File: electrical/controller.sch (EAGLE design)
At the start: 27 parts, among them Q1 IRLIB9343PBF-ND, U1 MCP6002, U2 POLOLU_U1V11F5, U3 MCP4725, U4 MCP4725

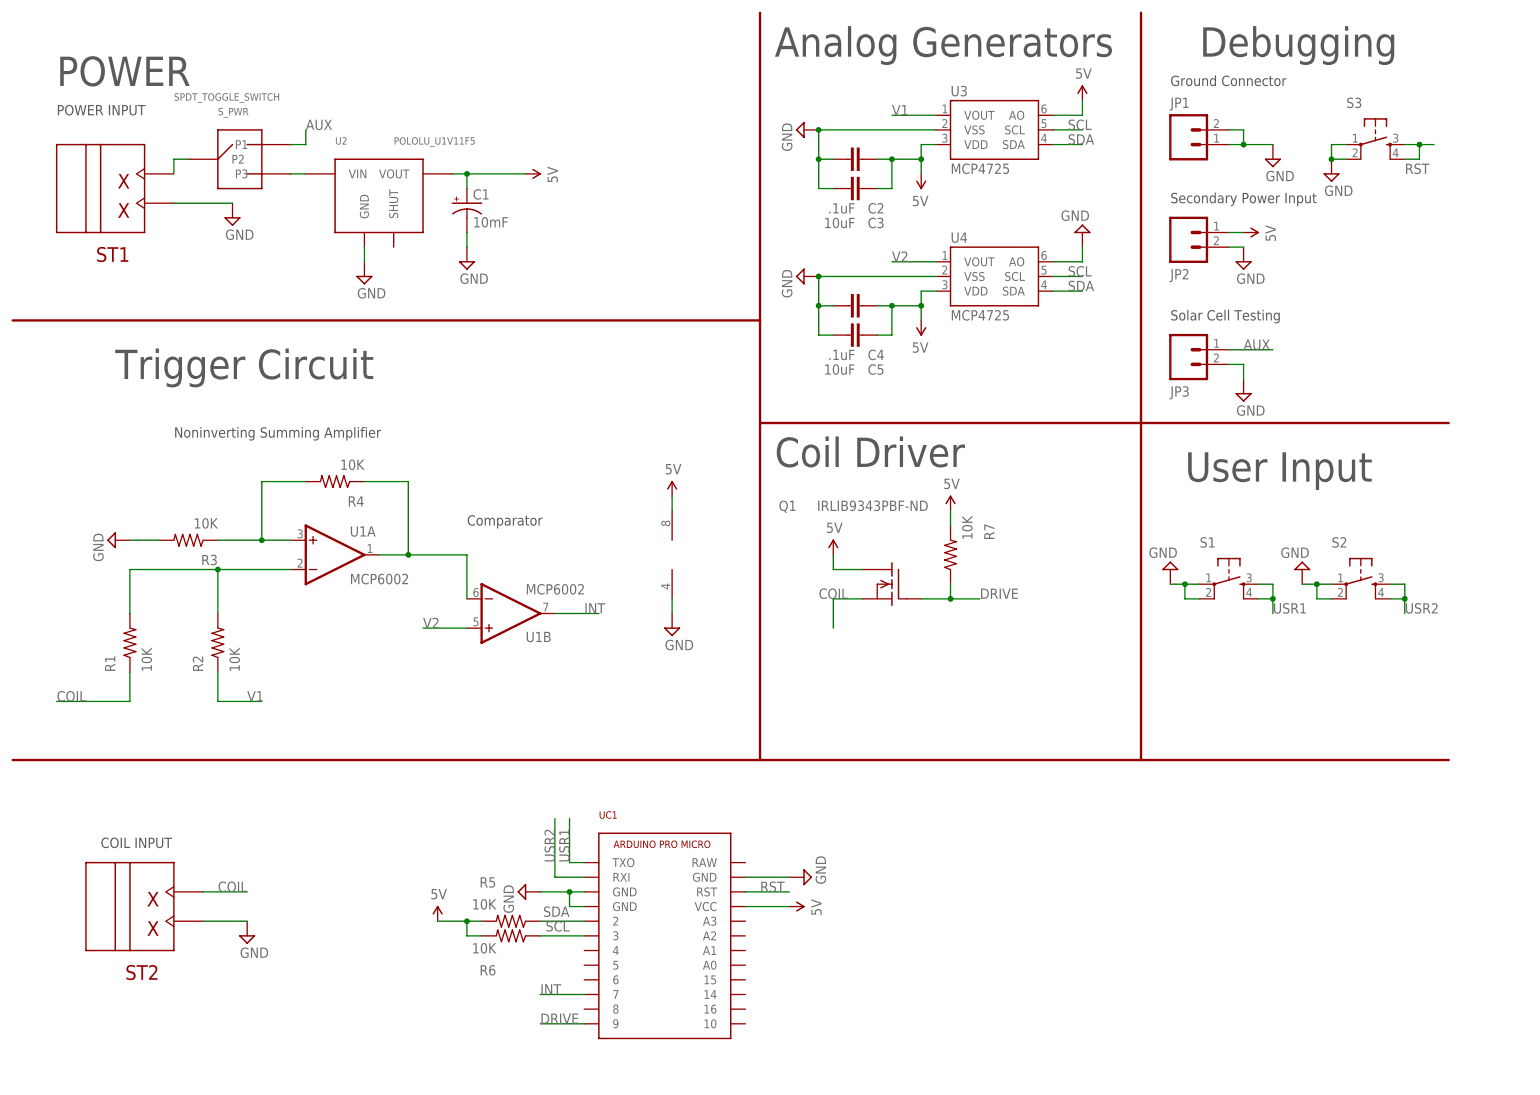
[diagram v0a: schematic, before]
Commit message: Rev B PCB changes
New parts, re-route.
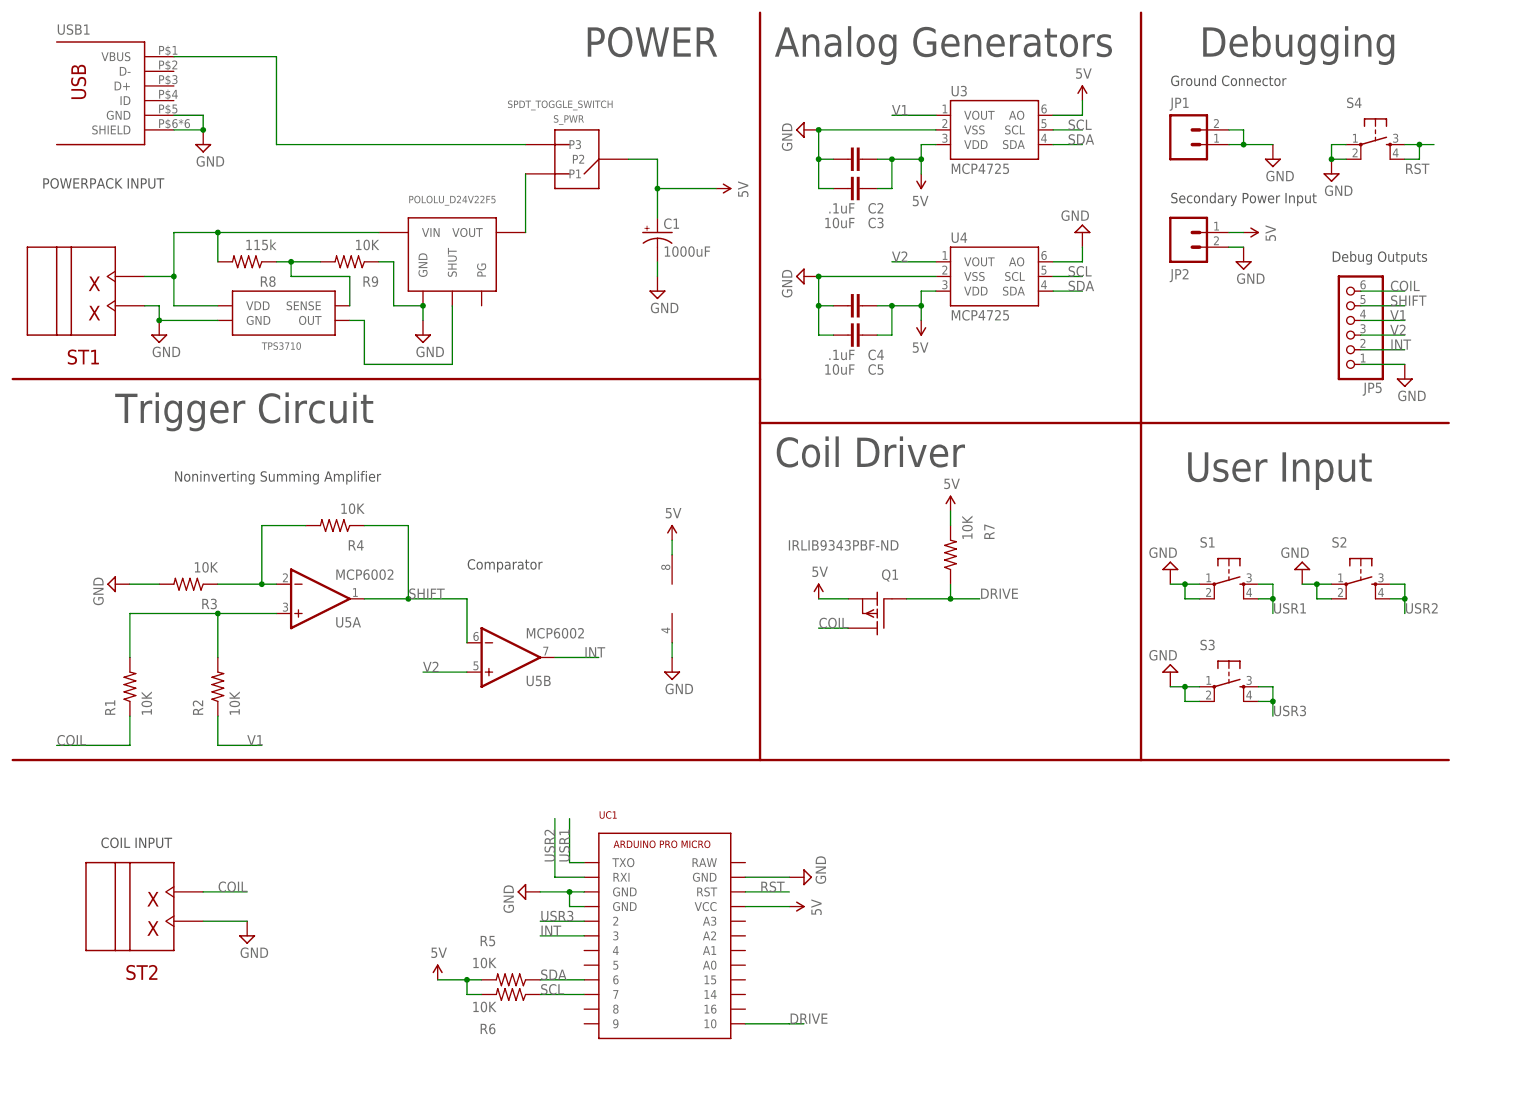
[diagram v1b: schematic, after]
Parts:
- removed JP3: (no value), pie:M02PTH
- added JP5: (no value), pinhead:PINHD-1X6
- added R8: 115k, pie:R-US_R0603
- added R9: 10K, pie:R-US_R0603
- added S4: (no value), pie:TAC_SWITCHPTH
- added U5: MCP6002, linear:MCP602P
- added USB1: USB-OTGMICRO-AB, pie:USB-OTGMICRO-AB
- C1: value 10mF -> 1000uF; device SparkFun-Capacitors:CAP_POLPTH3 -> SparkFun-Capacitors:CAP_POLPTH4
- Q1: device transistor-fet:BUZ20 -> transistor-fet:IRF9530
- U1: value MCP6002 -> POLOLU_D24V22F5; device linear:MCP602P -> custom_parts:POLOLU_D24V22F5
- U2: value POLOLU_U1V11F5 -> TPS3710; device custom_parts:POLOLU_U1V11F5 -> custom_parts:TPS3710
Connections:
- removed net AUX: JP3.1, S_PWR.P1
- new net N$1: U1.SHUT, U2.OUT
- new net N$6: R8.1, R9.2, U2.SENSE
- new net SHIFT: JP5.5, R4.1, U5A.OUT, U5B.-IN
- new net USR3: S3.3, S3.4, UC1.2
- net 5V: now also Q1.S, S_PWR.P2, U5P.V+; no longer Q1.D, U1P.V+, U2.VOUT
- net COIL: now also JP5.6, Q1.D; no longer Q1.S
- net DRIVE: now also UC1.10; no longer UC1.9
- net GND: now also JP5.1, R9.1, S4.1, S4.2, U1.GND, U5P.V-, USB1.GND, USB1.SHIELD; no longer JP3.2, U1P.V-
- net INT: now also JP5.2, U5B.OUT, UC1.3; no longer U1B.OUT, UC1.7
- net N$2: now also S_PWR.P3, USB1.VBUS; no longer R4.1, U1A.OUT, U1B.-IN
- net N$3: now also S_PWR.P1, U1.VOUT; no longer S_PWR.P3, U2.VIN
- net N$4: now also U5A.+IN; no longer U1A.-IN
- net N$5: now also U5A.-IN; no longer U1A.+IN
- net RST: now also S4.3, S4.4; no longer S3.3, S3.4
- net SCL: now also UC1.7; no longer UC1.3
- net SDA: now also UC1.6; no longer UC1.2
- net V1: now also JP5.4
- net V2: now also JP5.3, U5B.+IN; no longer U1B.+IN
- net VBAT: now also R8.2, U1.VIN, U2.VDD; no longer S_PWR.P2
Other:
- note added: "Debug Outputs"
- note added: "POWERPACK INPUT"
- note removed: "POWER INPUT"
- note removed: "Solar Cell Testing"
- moved on the sheet: C1, Q1, R1, R2, R3, R4, R5, R6, S3, ST1, S_PWR

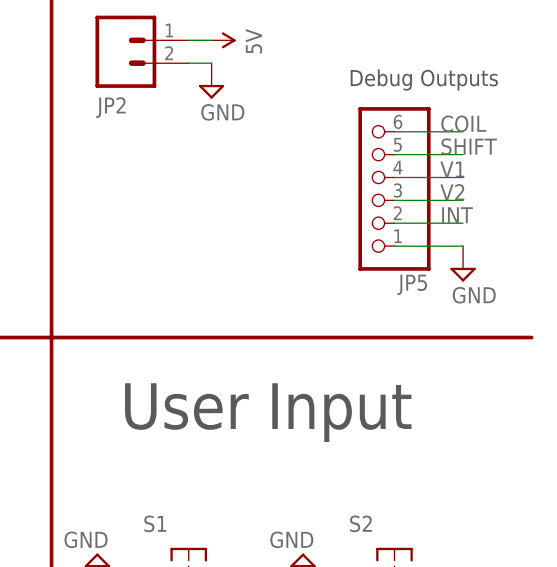
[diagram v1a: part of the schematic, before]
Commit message: Rename JP5 to JP3
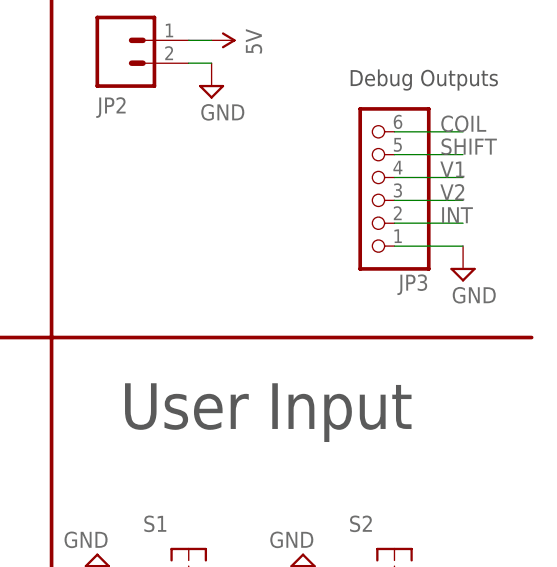
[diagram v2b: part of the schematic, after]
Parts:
- renumbered JP5 to JP3
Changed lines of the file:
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@@
 <part name="U$1" library="pie" deviceset="5V" device=""/>
 <part name="SUPPLY12" library="pie" deviceset="GND" device=""/>
-<part name="JP5" library="pinhead" deviceset="PINHD-1X6" device=""/>
+<part name="JP3" library="pinhead" deviceset="PINHD-1X6" device=""/>
 <part name="SUPPLY18" library="pie" deviceset="GND" device=""/>
 <part name="Q1" library="transistor-fet" deviceset="IRF9530" device="" value="IRLIB9343PBF-ND "/>
@@
 <instance part="U$1" gate="G$1" x="162.56" y="99.06"/>
 <instance part="SUPPLY12" gate="GND" x="185.42" y="147.32" rot="R180"/>
-<instance part="JP5" gate="A" x="231.14" y="132.08" rot="R180"/>
+<instance part="JP3" gate="A" x="231.14" y="132.08" rot="R180"/>
 <instance part="SUPPLY18" gate="GND" x="241.3" y="121.92"/>
 <instance part="Q1" gate="G$1" x="149.86" y="81.28" smashed="yes" rot="R180">
@@
 </segment>
 <segment>
-<pinref part="JP5" gate="A" pin="1"/>
+<pinref part="JP3" gate="A" pin="1"/>
 <wire x1="233.68" y1="124.46" x2="241.3" y2="124.46" width="0.1524" layer="91"/>
 <pinref part="SUPPLY18" gate="GND" pin="GND"/>
@@
 <wire x1="233.68" y1="137.16" x2="241.3" y2="137.16" width="0.1524" layer="91"/>
 <label x="238.76" y="137.16" size="1.778" layer="95"/>
-<pinref part="JP5" gate="A" pin="6"/>
+<pinref part="JP3" gate="A" pin="6"/>
 </segment>
 <segment>
@@
 <wire x1="233.68" y1="134.62" x2="241.3" y2="134.62" width="0.1524" layer="91"/>
 <label x="238.76" y="134.62" size="1.778" layer="95"/>
-<pinref part="JP5" gate="A" pin="5"/>
+<pinref part="JP3" gate="A" pin="5"/>
 </segment>
 </net>
@@
 <wire x1="233.68" y1="129.54" x2="241.3" y2="129.54" width="0.1524" layer="91"/>
 <label x="238.76" y="129.54" size="1.778" layer="95"/>
-<pinref part="JP5" gate="A" pin="3"/>
+<pinref part="JP3" gate="A" pin="3"/>
 </segment>
 </net>
@@
 <wire x1="233.68" y1="132.08" x2="241.3" y2="132.08" width="0.1524" layer="91"/>
 <label x="238.76" y="132.08" size="1.778" layer="95"/>
-<pinref part="JP5" gate="A" pin="4"/>
+<pinref part="JP3" gate="A" pin="4"/>
 </segment>
 </net>
@@
 <wire x1="233.68" y1="127" x2="241.3" y2="127" width="0.1524" layer="91"/>
 <label x="238.76" y="127" size="1.778" layer="95"/>
-<pinref part="JP5" gate="A" pin="2"/>
-</segment>
-<segment>
+<pinref part="JP3" gate="A" pin="2"/>
+</segment>
+<segment>

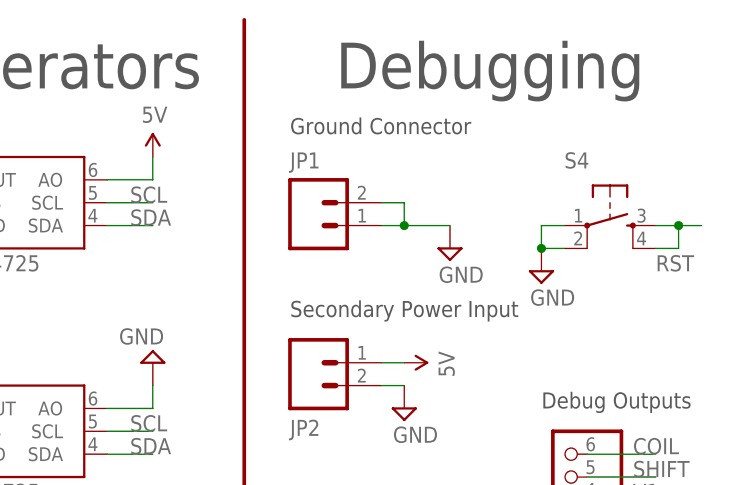
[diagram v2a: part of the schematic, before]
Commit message: Fix Rev B erratta
Hole sizes for screw terminals
Pour clearance
Silkscreen Fixes
Revision Numbers
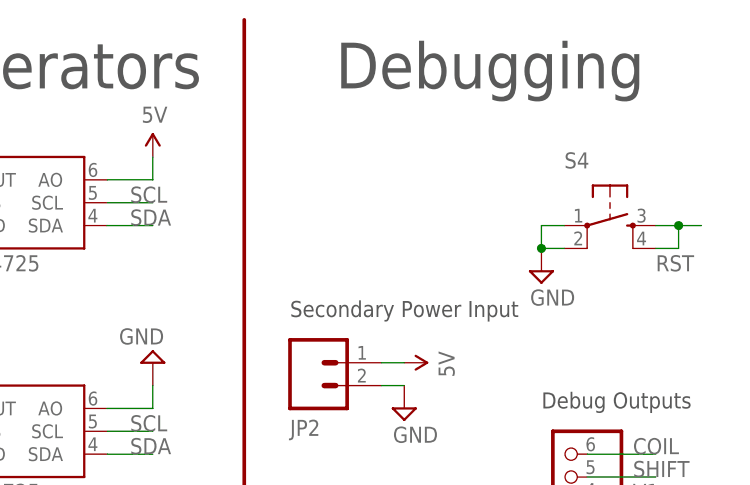
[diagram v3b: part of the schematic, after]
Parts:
- removed JP1: (no value), pie:M02PTH
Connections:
- net GND: no longer JP1.1, JP1.2
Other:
- note removed: "Ground Connector"
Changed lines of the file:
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@@
 <attributes>
 <attribute name="AUTHOR" value="Douglas Hutchings"/>
-<attribute name="REVISION" value="A"/>
+<attribute name="REVISION" value="C"/>
 </attributes>
 <variantdefs>
@@
 <part name="C5" library="pie" deviceset="CAP" device="0805" value="10uF"/>
 <part name="C4" library="pie" deviceset="CAP" device="0603-CAP" value=".1uF"/>
-<part name="JP1" library="pie" deviceset="M02" device="PTH"/>
-<part name="SUPPLY11" library="pie" deviceset="GND" device=""/>
 <part name="U$9" library="pie" deviceset="5V" device=""/>
 <part name="R5" library="pie" deviceset="R-US_" device="R0603" value="10K"/>
@@
 <wire x1="195.58" y1="114.3" x2="195.58" y2="185.42" width="0.4064" layer="94"/>
 <text x="205.74" y="177.8" size="5.08" layer="97">Debugging</text>
-<text x="200.66" y="172.72" size="1.778" layer="97">Ground Connector</text>
 <text x="132.08" y="106.68" size="5.08" layer="97">Coil Driver</text>
 <wire x1="195.58" y1="114.3" x2="248.92" y2="114.3" width="0.4064" layer="94"/>
@@
 <attribute name="VALUE" x="146.05" y="127" size="1.778" layer="96" rot="R180"/>
 </instance>
-<instance part="JP1" gate="G$1" x="203.2" y="165.1"/>
-<instance part="SUPPLY11" gate="GND" x="218.44" y="160.02"/>
 <instance part="U$9" gate="G$1" x="213.36" y="147.32" rot="R270"/>
 <instance part="R5" gate="G$1" x="86.36" y="17.78" smashed="yes" rot="R180">
@@
 </segment>
 <segment>
-<pinref part="JP1" gate="G$1" pin="2"/>
-<wire x1="210.82" y1="165.1" x2="213.36" y2="165.1" width="0.1524" layer="91"/>
-<wire x1="213.36" y1="165.1" x2="213.36" y2="162.56" width="0.1524" layer="91"/>
-<pinref part="SUPPLY11" gate="GND" pin="GND"/>
-<wire x1="213.36" y1="162.56" x2="218.44" y2="162.56" width="0.1524" layer="91"/>
-<pinref part="JP1" gate="G$1" pin="1"/>
-<wire x1="213.36" y1="162.56" x2="210.82" y2="162.56" width="0.1524" layer="91"/>
-<junction x="213.36" y="162.56"/>
-</segment>
-<segment>
